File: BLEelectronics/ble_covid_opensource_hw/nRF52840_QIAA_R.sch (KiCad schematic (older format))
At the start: 24 parts, among them U6 nRF52840

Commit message: Schematic draft, working on Antenna layout.
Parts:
- added Y1: 32MHz, Crystal:Crystal_SMD_2016-4Pin_2.0x1.6mm, symbol Device:Crystal_GND24
- L1, L3: footprint (none) -> Inductor_SMD:L_0402_1005Metric
- L2: footprint (none) -> Inductor_SMD:L_0603_1608Metric
- L4: renamed from L?; footprint (none) -> Inductor_SMD:L_0603_1608Metric
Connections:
- wire segments 58 -> 62
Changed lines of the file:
@@
 F 0 "L1" V 2640 3000 50  0000 C CNN
 F 1 "L" V 2549 3000 50  0000 C CNN
-F 2 "" H 2450 3000 50  0001 C CNN
+F 2 "Inductor_SMD:L_0402_1005Metric" H 2450 3000 50  0001 C CNN
 F 3 "~" H 2450 3000 50  0001 C CNN
 	1    2450 3000
@@
 	1800 4600 1800 5000
 Connection ~ 1800 5000
-Wire Wire Line
-	2900 4600 2100 4600
-Wire Wire Line
-	2900 5000 2100 5000
 NoConn ~ 5500 3200
 NoConn ~ 5500 3300
@@
 F 0 "L2" H 5253 1396 50  0000 L CNN
 F 1 "10uH" H 5253 1305 50  0000 L CNN
-F 2 "" H 5200 1350 50  0001 C CNN
+F 2 "Inductor_SMD:L_0603_1608Metric" H 5200 1350 50  0001 C CNN
 F 3 "~" H 5200 1350 50  0001 C CNN
 	1    5200 1350
@@
 F 0 "L3" H 5253 1796 50  0000 L CNN
 F 1 "15nH" H 5253 1705 50  0000 L CNN
-F 2 "" H 5200 1750 50  0001 C CNN
+F 2 "Inductor_SMD:L_0402_1005Metric" H 5200 1750 50  0001 C CNN
 F 3 "~" H 5200 1750 50  0001 C CNN
 	1    5200 1750
@@
 	4100 1050 4100 1500
 $Comp
-L Device:L L?
+L Device:L L4
 U 1 1 5EC65BAC
 P 4350 1950
-F 0 "L?" V 4540 1950 50  0000 C CNN
+F 0 "L4" V 4540 1950 50  0000 C CNN
 F 1 "10uH" V 4449 1950 50  0000 C CNN
-F 2 "" H 4350 1950 50  0001 C CNN
+F 2 "Inductor_SMD:L_0603_1608Metric" H 4350 1950 50  0001 C CNN
 F 3 "~" H 4350 1950 50  0001 C CNN
 	1    4350 1950
@@
 NoConn ~ 5500 6800
 NoConn ~ 5500 6900
+$Comp
+L Device:Crystal_GND24 Y1
+U 1 1 5EC864DB
+P 2550 4800
+F 0 "Y1" V 2596 4556 50  0000 R CNN
+F 1 "32MHz" V 2505 4556 50  0000 R CNN
+F 2 "Crystal:Crystal_SMD_2016-4Pin_2.0x1.6mm" H 2550 4800 50  0001 C CNN
+F 3 "https://media.digikey.com/PDF/Data%20Sheets/NDK%20PDFs/NX2016AB-32MHZ%20ST2.pdf" H 2550 4800 50  0001 C CNN
+F 4 "NDK America, Inc." H 2550 4800 50  0001 C CNN "MFR"
+F 5 "NX2016AB-32MHZ ST2" H 2550 4800 50  0001 C CNN "MPN"
+F 6 "644-1119-1-ND" H 2550 4800 50  0001 C CNN "DPN"
+	1    2550 4800
+	0    -1   -1   0
+$EndComp
+Wire Wire Line
+	2550 4650 2550 4600
+Wire Wire Line
+	2550 4950 2550 5000
+$Comp
+L power:GND #PWR0102
+U 1 1 5EC8B834
+P 2750 4800
+AR Path="/5EA608FF/5EC8B834" Ref="#PWR0102"  Part="1"
+AR Path="/5EC8B834" Ref="#PWR?"  Part="1"
+F 0 "#PWR0102" H 2750 4550 50  0001 C CNN
+F 1 "GND" V 2755 4672 50  0000 R CNN
+F 2 "" H 2750 4800 50  0001 C CNN
+F 3 "" H 2750 4800 50  0001 C CNN
+	1    2750 4800
+	0    -1   -1   0
+$EndComp
+$Comp
+L power:GND #PWR0103
+U 1 1 5EC8CD02
+P 2350 4800
+AR Path="/5EA608FF/5EC8CD02" Ref="#PWR0103"  Part="1"
+AR Path="/5EC8CD02" Ref="#PWR?"  Part="1"
+F 0 "#PWR0103" H 2350 4550 50  0001 C CNN
+F 1 "GND" V 2355 4672 50  0000 R CNN
+F 2 "" H 2350 4800 50  0001 C CNN
+F 3 "" H 2350 4800 50  0001 C CNN
+	1    2350 4800
+	0    1    1    0
+$EndComp
+Connection ~ 2550 4600
+Wire Wire Line
+	2550 4600 2900 4600
+Connection ~ 2550 5000
+Wire Wire Line
+	2550 5000 2900 5000
+Wire Wire Line
+	2100 4600 2550 4600
+Wire Wire Line
+	2100 5000 2550 5000
 $EndSCHEMATC

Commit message: Partial progress on hw mvp 1b.
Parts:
- added D1: LED, symbol Device:LED
- added D2: LED_ABRG, symbol Device:LED_ABRG
- added R11: 2k2, symbol Device:R
- added R12: 390, symbol Device:R
- added R2: 220, symbol Device:R
- added R3: 1k2, symbol Device:R
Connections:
- net labels added: LED1, LED2_B, LED2_G, LED2_R, SIO3, SW1
- wire segments 62 -> 79
- no-connect marks 37 -> 36
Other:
- note added: "CS - P0.17\nCLK - P0.19\nSI - P0.20\nSO - P0.21\nWP - P0.22\nSIO3/HOLD/RESET(pin7) - P0.23\nPinouts from development board schematic\n"
- note added: "Confirmed no pull-up/down\nresistors for SPI protocol\nAdd 100nF cap between \nGND and VCC"
- note added: "GPIO not marked for any other function or low frequency include P0.13, 15, 17, 20, 22, 24, P1.00"
- note added: "LEDs are active low, which means that writing a logical \nzero '0' to the output pin will illuminate the LED.\nLED footprint and component TBD. Resistor footprint?"
- note added: "Low Freq XTAL"
- note added: "P1.06 are active low, they don't have an internal pullup resistor. \nThe switch must be configured to have a 10k pull-up resstor. \nWhen the button is active the pin is connected to ground. \nDetails from Dongle User Guide pg 13"
- moved on the sheet: C21, C22
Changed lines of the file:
@@
 NoConn ~ 2900 6600
 NoConn ~ 2900 6700
-Text Label 5500 7000 0    50   ~ 0
-RESET
-Text Label 5500 4200 0    50   ~ 0
+Text Label 5500 4400 0    50   ~ 0
 WP
 Text Label 5500 4600 0    50   ~ 0
 SDA
-Text Label 5500 5500 0    50   ~ 0
+Text Label 5500 3800 0    50   ~ 0
 SCL
+Text Label 5500 4100 0    50   ~ 0
+SCLK
+Text Label 5500 4200 0    50   ~ 0
+SI
 Text Label 5500 4000 0    50   ~ 0
-SCLK
-Text Label 5500 4400 0    50   ~ 0
-SI
-Text Label 5500 3600 0    50   ~ 0
 CS
-Text Label 5500 3800 0    50   ~ 0
+Text Label 5500 4300 0    50   ~ 0
 SO
 $Comp
@@
 NoConn ~ 5500 3300
 NoConn ~ 5500 3000
-NoConn ~ 5500 3100
 NoConn ~ 5500 3400
-NoConn ~ 5500 3500
 NoConn ~ 5500 3700
 NoConn ~ 5500 3900
@@
 Text Label 2500 6500 0    50   ~ 0
 RESET
-Text Label 5500 4100 0    50   ~ 0
-RESET
-Text Label 5500 4300 0    50   ~ 0
-RESET
 Text Label 5500 4500 0    50   ~ 0
-RESET
-Text Label 5500 4700 0    50   ~ 0
-RESET
+SIO3
 Text Label 2800 3350 0    50   ~ 0
 VSS_PA
@@
 	0    -1   -1   0
 $EndComp
-$Comp
-L MCU_Nordic:nRF52840 U6
-U 1 1 5EC0DD0A
-P 4200 4800
-AR Path="/5EA608FF/5EC0DD0A" Ref="U6"  Part="1"
-AR Path="/5EC0DD0A" Ref="U?"  Part="1"
-F 0 "U6" H 4150 4650 50  0000 C CNN
-F 1 "nRF52840" H 4150 4550 50  0000 C CNN
-F 2 "Package_DFN_QFN:Nordic_AQFN-73-1EP_7x7mm_P0.5mm" H 4200 1900 50  0001 C CNN
-F 3 "http://infocenter.nordicsemi.com/topic/com.nordic.infocenter.nrf52/dita/nrf52/chips/nrf52840.html" H 3550 6700 50  0001 C CNN
-	1    4200 4800
-	1    0    0    -1
-$EndComp
 Text Label 5900 2100 0    50   ~ 0
 VSS
@@
 L Device:C C?
 U 1 1 5EC5C964
-P 6450 2300
+P 7200 2300
 AR Path="/5EC5C964" Ref="C?"  Part="1"
 AR Path="/5EA608FF/5EC5C964" Ref="C21"  Part="1"
-F 0 "C21" V 6702 2300 50  0000 C CNN
-F 1 "12pF" V 6611 2300 50  0000 C CNN
-F 2 "Capacitor_SMD:C_0603_1608Metric" H 6488 2150 50  0001 C CNN
-F 3 "~" H 6450 2300 50  0001 C CNN
-	1    6450 2300
+F 0 "C21" V 7452 2300 50  0000 C CNN
+F 1 "12pF" V 7361 2300 50  0000 C CNN
+F 2 "Capacitor_SMD:C_0603_1608Metric" H 7238 2150 50  0001 C CNN
+F 3 "~" H 7200 2300 50  0001 C CNN
+	1    7200 2300
 	0    1    1    0
 $EndComp
@@
 L power:GND #PWR024
 U 1 1 5EC5C96A
-P 6600 2850
+P 7350 2850
 AR Path="/5EA608FF/5EC5C96A" Ref="#PWR024"  Part="1"
 AR Path="/5EC5C96A" Ref="#PWR?"  Part="1"
-F 0 "#PWR024" H 6600 2600 50  0001 C CNN
-F 1 "GND" V 6605 2722 50  0000 R CNN
-F 2 "" H 6600 2850 50  0001 C CNN
-F 3 "" H 6600 2850 50  0001 C CNN
-	1    6600 2850
+F 0 "#PWR024" H 7350 2600 50  0001 C CNN
+F 1 "GND" V 7355 2722 50  0000 R CNN
+F 2 "" H 7350 2850 50  0001 C CNN
+F 3 "" H 7350 2850 50  0001 C CNN
+	1    7350 2850
 	1    0    0    -1
 $EndComp
@@
 L Device:C C?
 U 1 1 5EC5C970
-P 6450 2700
+P 7200 2700
 AR Path="/5EC5C970" Ref="C?"  Part="1"
 AR Path="/5EA608FF/5EC5C970" Ref="C22"  Part="1"
-F 0 "C22" V 6702 2700 50  0000 C CNN
-F 1 "12pF" V 6611 2700 50  0000 C CNN
-F 2 "Capacitor_SMD:C_0603_1608Metric" H 6488 2550 50  0001 C CNN
-F 3 "~" H 6450 2700 50  0001 C CNN
-	1    6450 2700
-	0    1    1    0
-$EndComp
-Wire Wire Line
-	6600 2850 6600 2700
-Wire Wire Line
-	6600 2700 6600 2300
-Wire Wire Line
-	5500 2300 6300 2300
-Connection ~ 6600 2700
+F 0 "C22" V 7452 2700 50  0000 C CNN
+F 1 "12pF" V 7361 2700 50  0000 C CNN
+F 2 "Capacitor_SMD:C_0603_1608Metric" H 7238 2550 50  0001 C CNN
+F 3 "~" H 7200 2700 50  0001 C CNN
+	1    7200 2700
+	0    1    1    0
+$EndComp
+Wire Wire Line
+	7350 2850 7350 2700
+Wire Wire Line
+	7350 2700 7350 2300
+Connection ~ 7350 2700
 Wire Wire Line
 	5500 2400 6300 2400
@@
 NoConn ~ 5500 2700
 NoConn ~ 5500 2800
-NoConn ~ 5500 2900
 NoConn ~ 5500 5600
 NoConn ~ 5500 5700
@@
 NoConn ~ 5500 5900
 NoConn ~ 5500 6000
-NoConn ~ 5500 6100
 NoConn ~ 5500 6200
-NoConn ~ 5500 6400
 NoConn ~ 5500 6300
 NoConn ~ 5500 6500
@@
 Wire Wire Line
 	2100 5000 2550 5000
+Text Notes 6100 4450 0    50   ~ 0
+P1.15 is a low frequency GPIO (<10kHz)
+Text Notes 6100 4850 0    50   ~ 0
+Confirmed no pull-up/down\nresistors for SPI protocol\nAdd 100nF cap between \nGND and VCC
+Text Notes 6100 5000 0    50   ~ 0
+GPIO not marked for any other function or low frequency include P0.13, 15, 17, 20, 22, 24, P1.00
+Text Notes 6100 4300 0    50   ~ 0
+CS - P0.17\nCLK - P0.19\nSI - P0.20\nSO - P0.21\nWP - P0.22\nSIO3/HOLD/RESET(pin7) - P0.23\nPinouts from development board schematic\n
+NoConn ~ 5500 3600
+NoConn ~ 5500 4700
+NoConn ~ 5500 5500
+$Comp
+L MCU_Nordic:nRF52840 U6
+U 1 1 5EC0DD0A
+P 4200 4800
+AR Path="/5EA608FF/5EC0DD0A" Ref="U6"  Part="1"
+AR Path="/5EC0DD0A" Ref="U?"  Part="1"
+F 0 "U6" H 4150 4650 50  0000 C CNN
+F 1 "nRF52840" H 4150 4550 50  0000 C CNN
+F 2 "Package_DFN_QFN:Nordic_AQFN-73-1EP_7x7mm_P0.5mm" H 4200 1900 50  0001 C CNN
+F 3 "http://infocenter.nordicsemi.com/topic/com.nordic.infocenter.nrf52/dita/nrf52/chips/nrf52840.html" H 3550 6700 50  0001 C CNN
+	1    4200 4800
+	1    0    0    -1
+$EndComp
+Text Label 5500 3500 0    50   ~ 0
+LED2_B
+Text Label 5500 6400 0    50   ~ 0
+LED2_G
+Text Label 5500 3100 0    50   ~ 0
+LED2_R
+Text Label 5500 2900 0    50   ~ 0
+LED1
+NoConn ~ 5500 7000
+Wire Wire Line
+	5500 6100 6000 6100
+Text Label 6000 6100 0    50   ~ 0
+SW1
+Text Notes 6600 6150 0    50   ~ 0
+P1.06 are active low, they don't have an internal pullup resistor. \nThe switch must be configured to have a 10k pull-up resstor. \nWhen the button is active the pin is connected to ground. \nDetails from Dongle User Guide pg 13
+$Comp
+L Device:R R2
+U 1 1 5EAA0A31
+P 9500 850
+F 0 "R2" V 9293 850 50  0000 C CNN
+F 1 "220" V 9384 850 50  0000 C CNN
+F 2 "" V 9430 850 50  0001 C CNN
+F 3 "~" H 9500 850 50  0001 C CNN
+	1    9500 850
+	0    1    1    0
+$EndComp
+$Comp
+L Device:LED D1
+U 1 1 5EAAF1B1
+P 10100 850
+F 0 "D1" H 10093 1066 50  0000 C CNN
+F 1 "LED" H 10093 975 50  0000 C CNN
+F 2 "" H 10100 850 50  0001 C CNN
+F 3 "~" H 10100 850 50  0001 C CNN
+	1    10100 850
+	1    0    0    -1
+$EndComp
+Wire Wire Line
+	9950 850  9650 850
+Wire Wire Line
+	10250 850  10400 850
+Text Label 10400 1150 0    50   ~ 0
+VDD_3V
+Wire Wire Line
+	10400 1450 10300 1450
+Wire Wire Line
+	10400 850  10400 1450
+Wire Wire Line
+	9800 1750 9650 1750
+Wire Wire Line
+	9800 1650 9800 1750
+Wire Wire Line
+	9900 1650 9800 1650
+Wire Wire Line
+	9650 1450 9900 1450
+Wire Wire Line
+	9800 1150 9650 1150
+Wire Wire Line
+	9800 1250 9800 1150
+Wire Wire Line
+	9900 1250 9800 1250
+$Comp
+L Device:LED_ABRG D2
+U 1 1 5EAAE258
+P 10100 1450
+F 0 "D2" H 10100 1947 50  0000 C CNN
+F 1 "LED_ABRG" H 10100 1856 50  0000 C CNN
+F 2 "" H 10100 1450 50  0001 C CNN
+F 3 "~" H 10100 1450 50  0001 C CNN
+	1    10100 1450
+	1    0    0    -1
+$EndComp
+Wire Wire Line
+	8950 1750 9350 1750
+Wire Wire Line
+	8950 1450 9350 1450
+Wire Wire Line
+	8950 1150 9350 1150
+$Comp
+L Device:R R12
+U 1 1 5EAA3DB3
+P 9500 1750
+F 0 "R12" V 9293 1750 50  0000 C CNN
+F 1 "390" V 9384 1750 50  0000 C CNN
+F 2 "" V 9430 1750 50  0001 C CNN
+F 3 "~" H 9500 1750 50  0001 C CNN
+	1    9500 1750
+	0    1    1    0
+$EndComp
+$Comp
+L Device:R R11
+U 1 1 5EAA2AE0
+P 9500 1450
+F 0 "R11" V 9293 1450 50  0000 C CNN
+F 1 "2k2" V 9384 1450 50  0000 C CNN
+F 2 "" V 9430 1450 50  0001 C CNN
+F 3 "~" H 9500 1450 50  0001 C CNN
+	1    9500 1450
+	0    1    1    0
+$EndComp
+$Comp
+L Device:R R3
+U 1 1 5EAA19A0
+P 9500 1150
+F 0 "R3" V 9293 1150 50  0000 C CNN
+F 1 "1k2" V 9384 1150 50  0000 C CNN
+F 2 "" V 9430 1150 50  0001 C CNN
+F 3 "~" H 9500 1150 50  0001 C CNN
+	1    9500 1150
+	0    1    1    0
+$EndComp
+Text Notes 8950 2050 0    50   ~ 0
+LEDs are active low, which means that writing a logical \nzero '0' to the output pin will illuminate the LED.\nLED footprint and component TBD. Resistor footprint?
+Text Label 8950 1750 0    50   ~ 0
+LED2_G
+Text Label 8950 1150 0    50   ~ 0
+LED2_R
+Text Label 8950 1450 0    50   ~ 0
+LED2_B
+Wire Wire Line
+	8950 850  9350 850
+Text Label 8950 850  0    50   ~ 0
+LED1
+Wire Wire Line
+	5500 2300 7050 2300
+Wire Wire Line
+	6300 2700 7050 2700
+Text Notes 6450 2550 0    50   ~ 0
+Low Freq XTAL
 $EndSCHEMATC

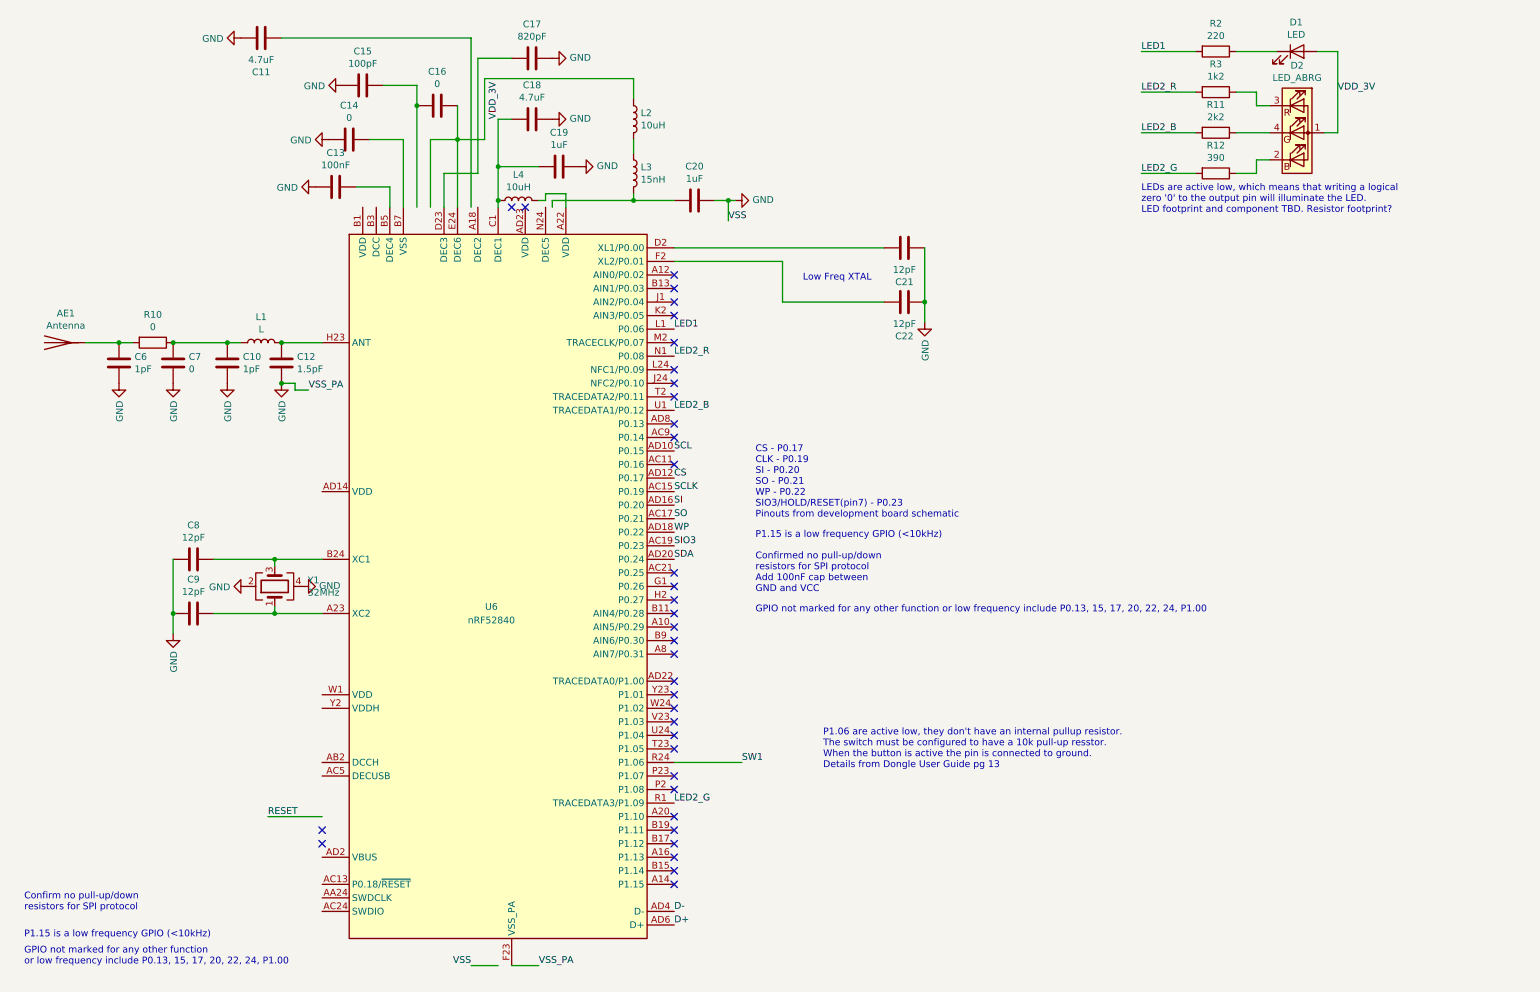
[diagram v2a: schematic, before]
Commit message: MVP 1b schematic almost ready for review.
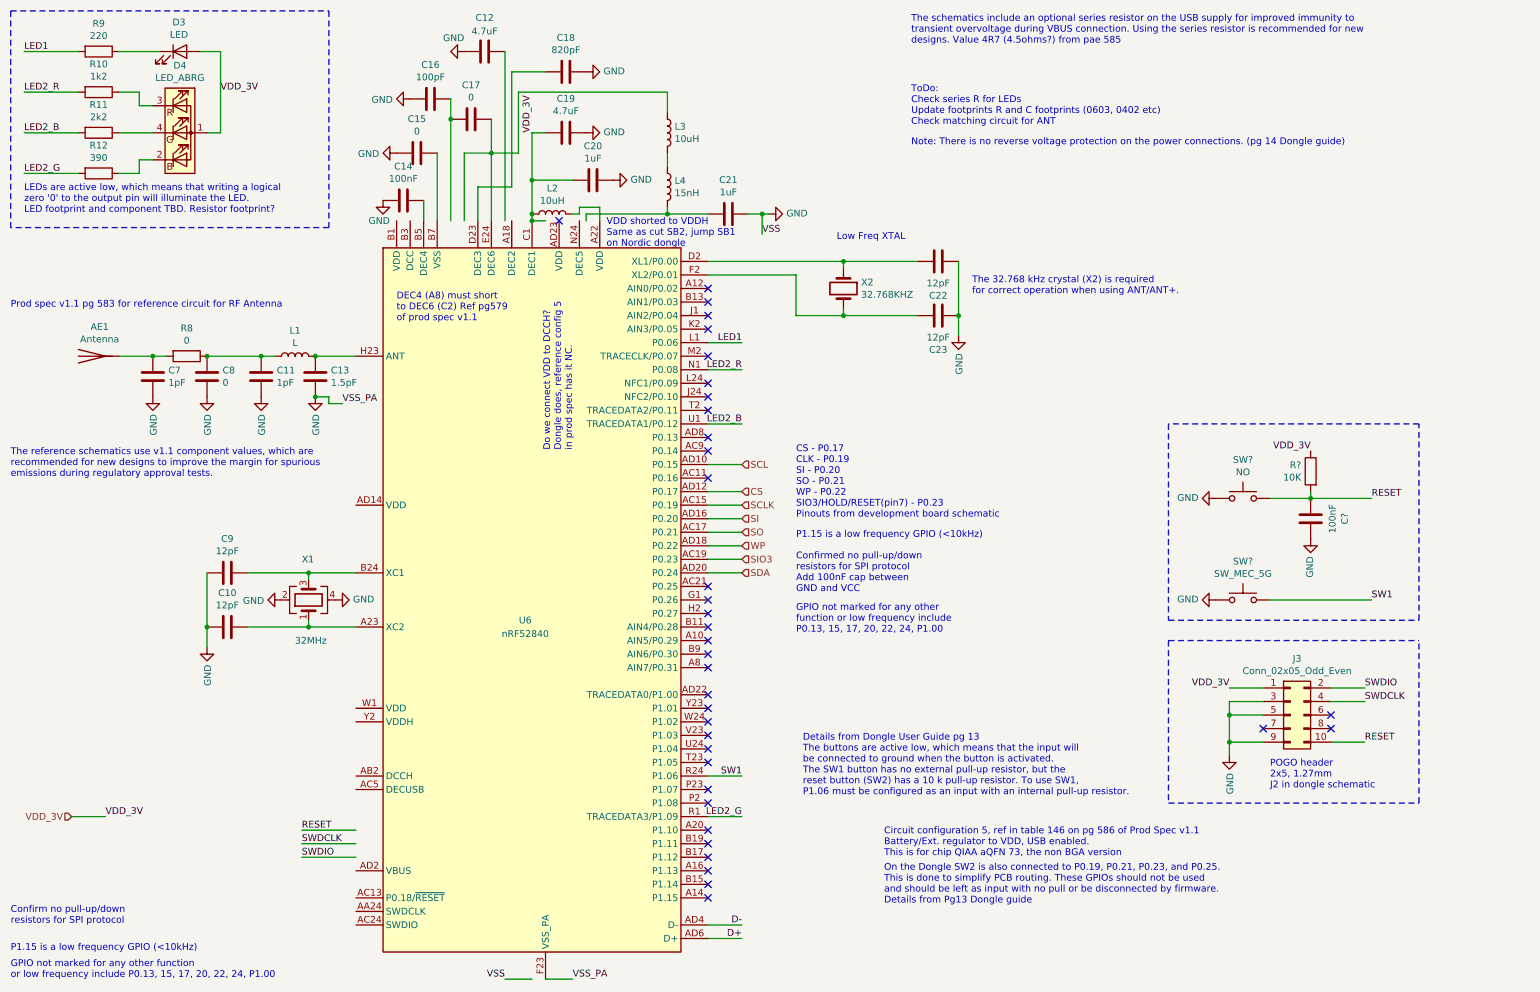
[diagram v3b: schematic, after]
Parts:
- added C?: 100nF, Capacitor_SMD:C_0603_1608Metric, symbol Device:C
- added J3: Conn_02x05_Odd_Even, 0my_footprints:TC2050-IDC-NLFP, symbol Connector_Generic:Conn_02x05_Odd_Even
- added R?: 10K, Resistor_SMD:R_0603_1608Metric_Pad1.05x0.95mm_HandSolder, symbol Device:R
- added SW?: NO, 0my_footprints:EVQP7A_J_B_K, symbol Switch:SW_MEC_5G
- added SW?: SW_MEC_5G, 0my_footprints:C&K_PTS810, symbol Switch:SW_MEC_5G
- added X2: 32.768KHZ, Crystal:Crystal_SMD_3215-2Pin_3.2x1.5mm, symbol Device:Crystal
- renumbered C9 to C10, C10 to C11, C11 to C12, C12 to C13, C13 to C14, C14 to C15, C15 to C16, C16 to C17, C17 to C18, C18 to C19, C19 to C20, C20 to C21, C21 to C22, C22 to C23, C6 to C7, C7 to C8, C8 to C9, D1 to D3, D2 to D4, L4 to L2, L2 to L3, L3 to L4, R3 to R10, R10 to R8, R2 to R9, Y1 to X1
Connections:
- net labels added: SWDCLK, SWDIO
- wire segments 79 -> 111
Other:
- note added: "Circuit configuration 5, ref in table 146 on pg 586 of Prod Spec v1.1\nBattery/Ext. regulator to VDD, USB enabled.\nThis is for chip QIAA aQFN 73, the non BGA version"
- note added: "DEC4 (A8) must short \nto DEC6 (C2) Ref pg579 \nof prod spec v1.1"
- note added: "Details from Dongle User Guide pg 13\nThe buttons are active low, which means that the input will \nbe connected to ground when the button is activated. \nThe SW1 button has no external pull-up resistor, but the \nreset button (SW2) has a 10 k pull-up resistor. To use SW1, \nP1.06 must be configured as an input with an internal pull-up resistor."
- note added: "Do we connect VDD to DCCH? \nDongle does, reference config 5 \nin prod spec has it NC."
- note added: "GPIO not marked for any other \nfunction or low frequency include \nP0.13, 15, 17, 20, 22, 24, P1.00"
- note added: "Note: There is no reverse voltage protection on the power connections. (pg 14 Dongle guide)"
- note added: "On the Dongle SW2 is also connected to P0.19, P0.21, P0.23, and P0.25. \nThis is done to simplify PCB routing. These GPIOs should not be used \nand should be left as input with no pull or be disconnected by firmware.\nDetails from Pg13 Dongle guide"
- note added: "POGO header\n2x5, 1.27mm\nJ2 in dongle schematic"
- note added: "Prod spec v1.1 pg 583 for reference circuit for RF Antenna"
- note added: "The 32.768 kHz crystal (X2) is required \nfor correct operation when using ANT/ANT+."
- note added: "The reference schematics use v1.1 component values, which are \nrecommended for new designs to improve the margin for spurious\nemissions during regulatory approval tests."
- note added: "The schematics include an optional series resistor on the USB supply for improved immunity to\ntransient overvoltage during VBUS connection. Using the series resistor is recommended for new\ndesigns. Value 4R7 (4.5ohms?) from pae 585"
- note added: "ToDo:\nCheck series R for LEDs\nUpdate footprints R and C footprints (0603, 0402 etc)\nCheck matching circuit for ANT\n"
- note added: "VDD shorted to VDDH\nSame as cut SB2, jump SB1\non Nordic dongle"
- note removed: "GPIO not marked for any other function or low frequency include P0.13, 15, 17, 20, 22, 24, P1.00"
- note removed: "P1.06 are active low, they don't have an internal pullup resistor. \nThe switch must be configured to have a 10k pull-up resstor. \nWhen the button is active the pin is connected to ground. \nDetails from Dongle User Guide pg 13"
- moved on the sheet: AE1, C10, C11, C12, C13, C14, C15, C16, C17, C18, C19, C20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
